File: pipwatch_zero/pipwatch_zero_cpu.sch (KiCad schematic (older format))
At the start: 39 parts, among them P401 CONN_1, P402 CONN_2, P403 CONN_10, Q401 BC849, SW401 TL1014BF180QG, SW402 FSM4JSMATR, SW403 FSM4JSMATR, SW404 FSM4JSMATR, U401 STM32F103RXT, X401 ABS25-32.768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

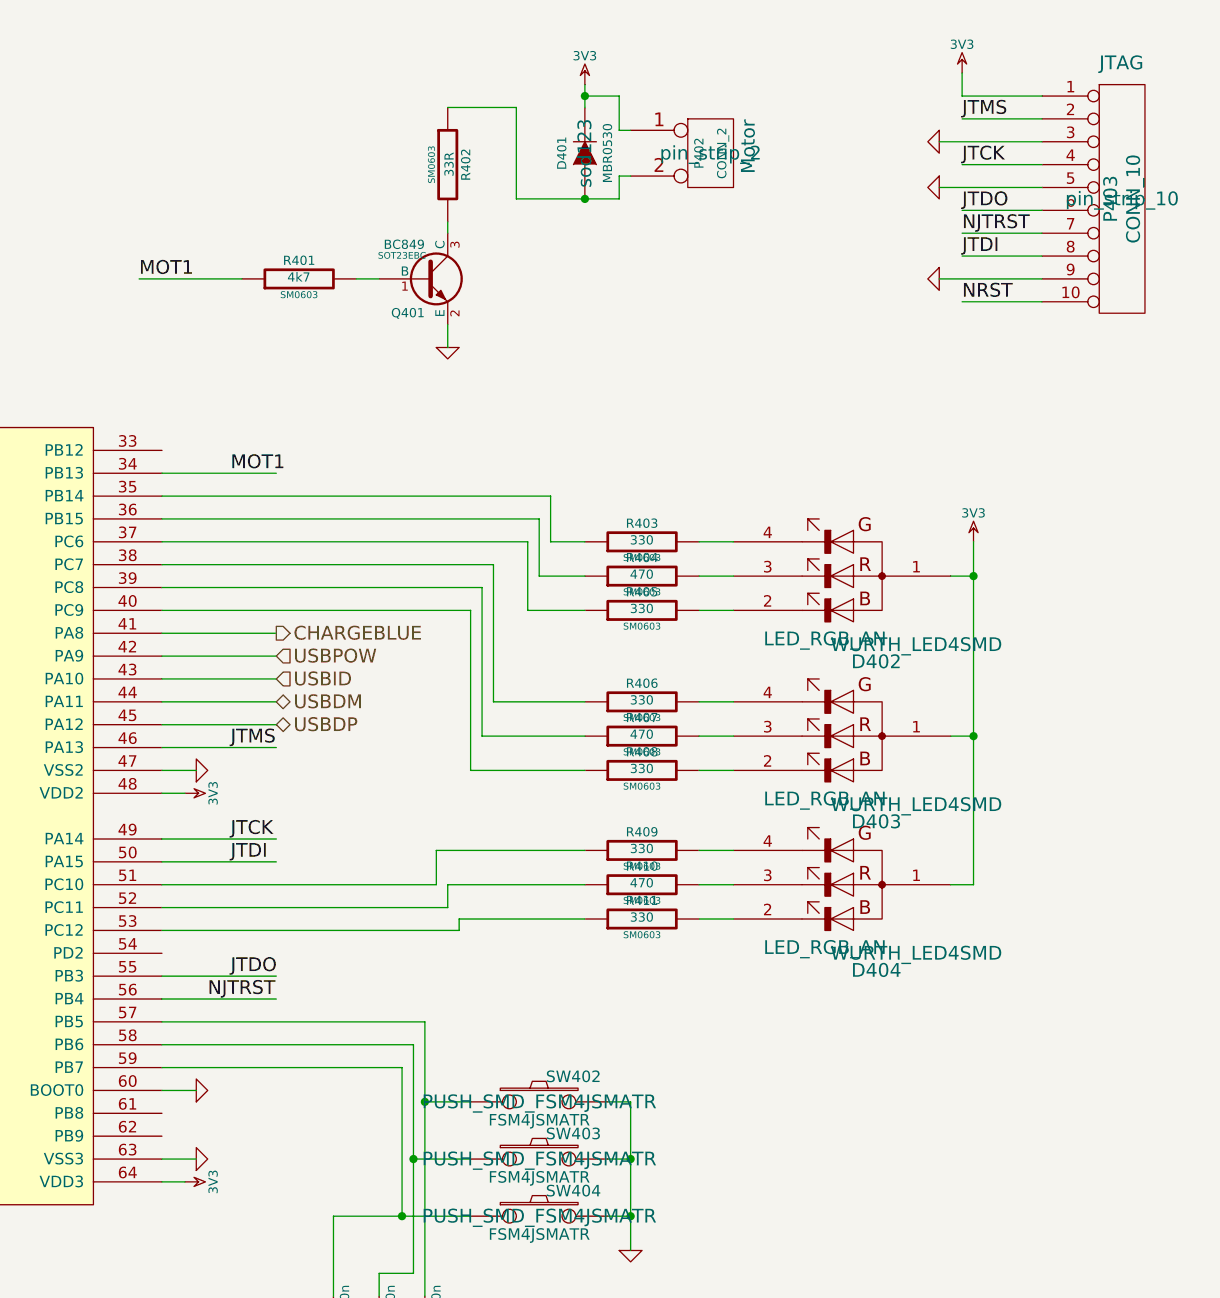
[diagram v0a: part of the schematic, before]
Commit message: pipwatch_zero layout complete
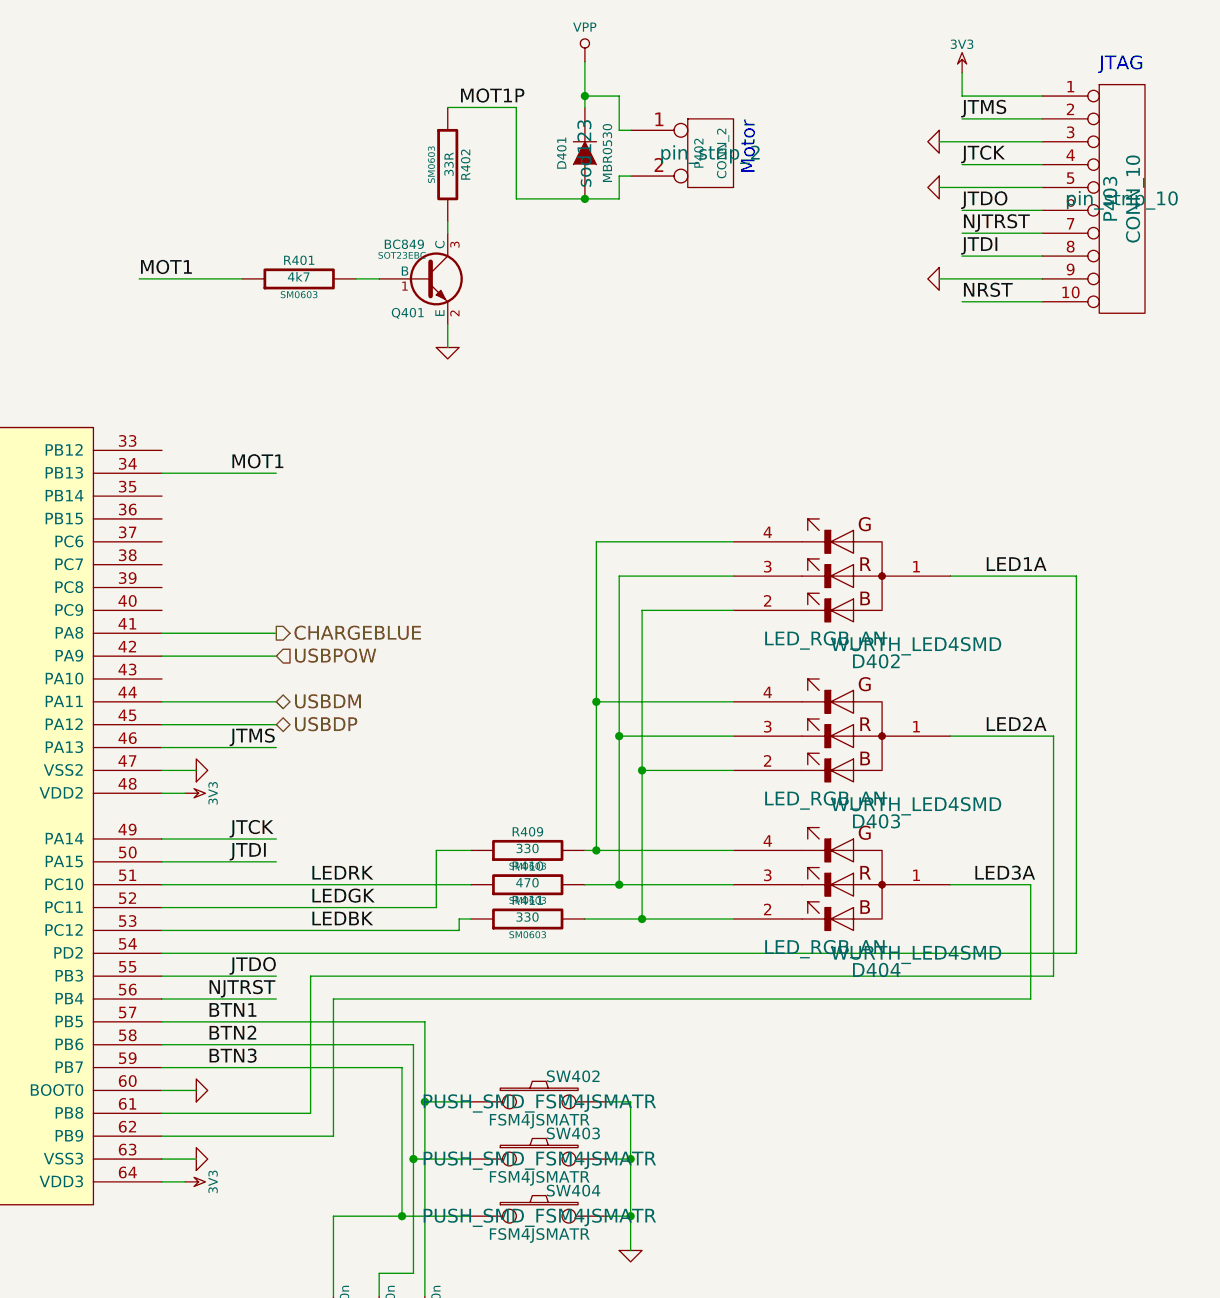
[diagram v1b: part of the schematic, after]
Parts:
- removed R403, R405, R406, R408: 330, SM0603, symbol R
- removed R404, R407: 470, SM0603, symbol R
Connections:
- net labels added: BTN1, BTN2, BTN3, LED1A, LED2A, LED3A, LEDBK, LEDGK, LEDRK, MOT1P, VPP
- net labels removed: USBID
- wire segments 161 -> 152
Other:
- moved on the sheet: R409, R410, R411

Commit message: pipwatch_zero hw02, sent to pragoboard
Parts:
- added SW405, SW406: SW_PUSH, PUSH_SMD_TS1107GS, symbol SW_PUSH
- P401: footprint 1PIN_SMD -> 1PIN_S_SMD
- P402: footprint pin_strip_2 -> do214aa
- P403: footprint pin_strip_10 -> PINARRAY_10P_2MM_SMD
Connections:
- wire segments 152 -> 156
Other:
- note added: "CPU XTAL\n8MHz"
- note added: "RTC XTAL\n32.768kHz"
- note added: "SW401/SW405/SW406 - alternative footprints and positions,\nmount only one of them!"
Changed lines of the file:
@@
 Sheet 4 5
 Title ""
-Date "31 aug 2014"
-Rev ""
+Date "3 sep 2014"
+Rev "HW02"
 Comp ""
 Comment1 ""
@@
 F 0 "SW401" H 3550 1910 50  0000 C CNN
 F 1 "TL1014BF180QG" H 3400 1720 50  0000 C CNN
-F 2 "PUSH_SMD_TL1014" H 3400 1800 60  0000 C CNN
+F 2 "PUSH_SMD_TL1014" H 3450 1650 39  0000 C CNN
 F 3 "~" H 3400 1800 60  0000 C CNN
 	1    3400 1800
@@
 F 0 "X401" H 2150 2650 60  0000 C CNN
 F 1 "ABS25-32.768" V 2150 3150 39  0000 C CNN
-F 2 "XTAL_ABS25" H 2150 2650 60  0000 C CNN
+F 2 "XTAL_ABS25" V 2250 3000 39  0000 C CNN
 F 3 "" H 2150 2650 60  0000 C CNN
 	1    2150 2650
@@
 F 0 "X402" H 2150 3450 60  0000 C CNN
 F 1 "CM309S8.000MABJ" V 2150 3950 39  0000 C CNN
-F 2 "XTAL_CM309S" H 2150 3450 60  0000 C CNN
+F 2 "XTAL_CM309S" V 2250 3850 39  0000 C CNN
 F 3 "" H 2150 3450 60  0000 C CNN
 	1    2150 3450
@@
 F 0 "C405" V 3350 2100 40  0000 L CNN
 F 1 "100n" V 3350 1800 40  0000 L CNN
-F 2 "SM0805" H 3438 1900 30  0000 C CNN
+F 2 "SM0805" V 3300 1900 30  0000 C CNN
 F 3 "~" H 3400 2050 60  0000 C CNN
 	1    3400 2050
@@
 	0    1    1    0
 $EndComp
-Text Notes 2950 1750 0    60   ~ 0
+Text Notes 2700 1400 0    60   ~ 0
 Reset
 $Comp
@@
 F 0 "P401" H 4180 2650 40  0000 L CNN
 F 1 "CONN_1" H 4100 2705 30  0001 C CNN
-F 2 "1PIN_SMD" H 4100 2650 60  0000 C CNN
+F 2 "1PIN_S_SMD" H 4100 2700 39  0000 C CNN
 F 3 "~" H 4100 2650 60  0000 C CNN
 	1    4100 2650
@@
 U 1 1 53D945BD
 P 9900 3100
-F 0 "D402" H 9925 2725 60  0000 C CNN
+F 0 "D402" H 9750 2950 60  0000 C CNN
 F 1 "LED_RGB_AN" H 10150 2825 60  0000 C CNN
-F 2 "WURTH_LED4SMD" H 9750 2800 60  0000 C CNN
+F 2 "WURTH_LED4SMD" H 9600 3050 39  0000 C CNN
 F 3 "~" H 9750 2800 60  0000 C CNN
 	1    9900 3100
@@
 U 1 1 53D945D9
 P 9900 3800
-F 0 "D403" H 9925 3425 60  0000 C CNN
+F 0 "D403" H 9750 3650 60  0000 C CNN
 F 1 "LED_RGB_AN" H 10150 3525 60  0000 C CNN
-F 2 "WURTH_LED4SMD" H 9750 3500 60  0000 C CNN
+F 2 "WURTH_LED4SMD" H 9600 3750 39  0000 C CNN
 F 3 "~" H 9750 3500 60  0000 C CNN
 	1    9900 3800
@@
 U 1 1 53D945DF
 P 9900 4450
-F 0 "D404" H 9925 4075 60  0000 C CNN
+F 0 "D404" H 9750 4300 60  0000 C CNN
 F 1 "LED_RGB_AN" H 10150 4175 60  0000 C CNN
-F 2 "WURTH_LED4SMD" H 9750 4150 60  0000 C CNN
+F 2 "WURTH_LED4SMD" H 9600 4400 39  0000 C CNN
 F 3 "~" H 9750 4150 60  0000 C CNN
 	1    9900 4450
@@
 F 0 "SW402" H 8550 5510 50  0000 C CNN
 F 1 "FSM4JSMATR" H 8400 5320 50  0000 C CNN
-F 2 "PUSH_SMD_FSM4JSMATR" H 8400 5400 60  0000 C CNN
+F 2 "PUSH_SMD_FSM4JSMATR" H 9000 5450 39  0000 C CNN
 F 3 "~" H 8400 5400 60  0000 C CNN
 	1    8400 5400
@@
 F 0 "SW403" H 8550 5760 50  0000 C CNN
 F 1 "FSM4JSMATR" H 8400 5570 50  0000 C CNN
-F 2 "PUSH_SMD_FSM4JSMATR" H 8400 5650 60  0000 C CNN
+F 2 "PUSH_SMD_FSM4JSMATR" H 9200 5650 39  0000 C CNN
 F 3 "~" H 8400 5650 60  0000 C CNN
 	1    8400 5650
@@
 F 0 "SW404" H 8550 6010 50  0000 C CNN
 F 1 "FSM4JSMATR" H 8400 5820 50  0000 C CNN
-F 2 "PUSH_SMD_FSM4JSMATR" H 8400 5900 60  0000 C CNN
+F 2 "PUSH_SMD_FSM4JSMATR" H 9200 5900 39  0000 C CNN
 F 3 "~" H 8400 5900 60  0000 C CNN
 	1    8400 5900
@@
 F 0 "P402" V 9100 1250 40  0000 C CNN
 F 1 "CONN_2" V 9200 1250 40  0000 C CNN
-F 2 "pin_strip_2" H 9150 1250 60  0000 C CNN
+F 2 "do214aa" H 9150 1250 60  0000 C CNN
 F 3 "~" H 9150 1250 60  0000 C CNN
 	1    9150 1250
@@
 F 0 "P403" V 10900 1450 60  0000 C CNN
 F 1 "CONN_10" V 11000 1450 60  0000 C CNN
-F 2 "pin_strip_10" H 10950 1450 60  0000 C CNN
+F 2 "PINARRAY_10P_2MM_SMD" H 10950 1450 60  0000 C CNN
 F 3 "~" H 10950 1450 60  0000 C CNN
 	1    10950 1450
@@
 	3700 1800 3850 1800
 Wire Wire Line
-	3850 1800 3850 3150
+	3850 1100 3850 3150
 Wire Wire Line
 	3850 3150 4400 3150
@@
 	3000 2050 3200 2050
 Wire Wire Line
-	3000 1800 3000 2050
+	3000 1100 3000 2050
 Wire Wire Line
 	3000 1800 3100 1800
@@
 	1    0    0    -1
 $EndComp
+$Comp
+L SW_PUSH SW405
+U 1 1 540768DA
+P 3400 1450
+F 0 "SW405" H 3550 1560 50  0000 C CNN
+F 1 "SW_PUSH" H 3400 1370 50  0000 C CNN
+F 2 "PUSH_SMD_TS1107GS" H 3350 1300 39  0000 C CNN
+F 3 "~" H 3400 1450 60  0000 C CNN
+	1    3400 1450
+	1    0    0    -1
+$EndComp
+Wire Wire Line
+	3100 1450 3000 1450
+Connection ~ 3000 1800
+Wire Wire Line
+	3700 1450 3850 1450
+Connection ~ 3850 1800
+Text Notes 3950 1050 0    60   ~ 0
+SW401/SW405/SW406 - alternative footprints and positions,\nmount only one of them!
+$Comp
+L SW_PUSH SW406
+U 1 1 54077385
+P 3400 1100
+F 0 "SW406" H 3550 1210 50  0000 C CNN
+F 1 "SW_PUSH" H 3400 1020 50  0000 C CNN
+F 2 "PUSH_SMD_TS1107GS" H 3350 950 39  0000 C CNN
+F 3 "~" H 3400 1100 60  0000 C CNN
+	1    3400 1100
+	1    0    0    -1
+$EndComp
+Wire Wire Line
+	3700 1100 3850 1100
+Connection ~ 3850 1450
+Wire Wire Line
+	3000 1100 3100 1100
+Connection ~ 3000 1450
+Text Notes 850  2650 0    60   ~ 0
+RTC XTAL\n32.768kHz
+Text Notes 850  3450 0    60   ~ 0
+CPU XTAL\n8MHz
 $EndSCHEMATC
